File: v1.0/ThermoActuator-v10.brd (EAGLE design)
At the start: 100 x 80 mm, 76 parts, among them IC1 ULN2003AD, IC2 LM358D, IC3 LM358D, IC4 LM358D, IC5 LM358D

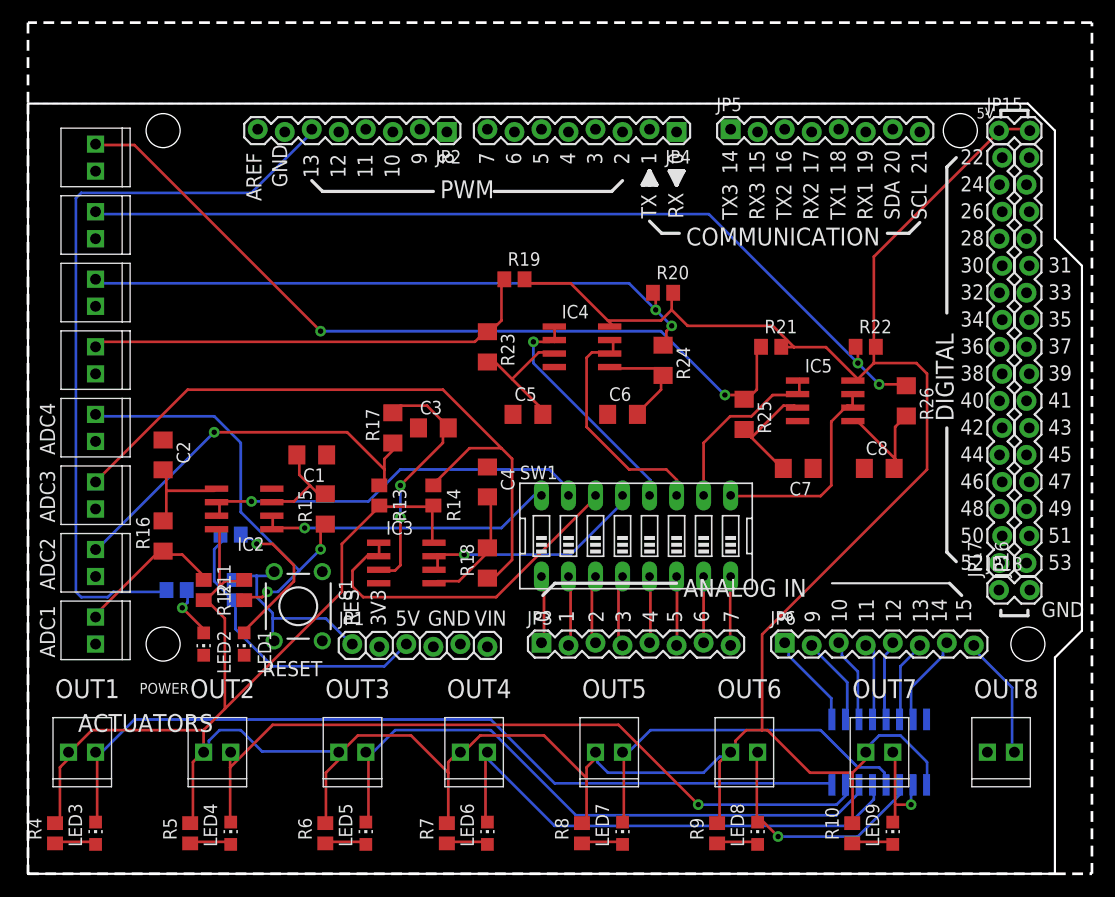
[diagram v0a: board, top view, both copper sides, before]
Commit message: local autorouting, no ripup *
almost done. Removed the reset button. Will not be used
on this shield (a higher shield will have it). Laying out
VDD route. Only local auto-route from now on
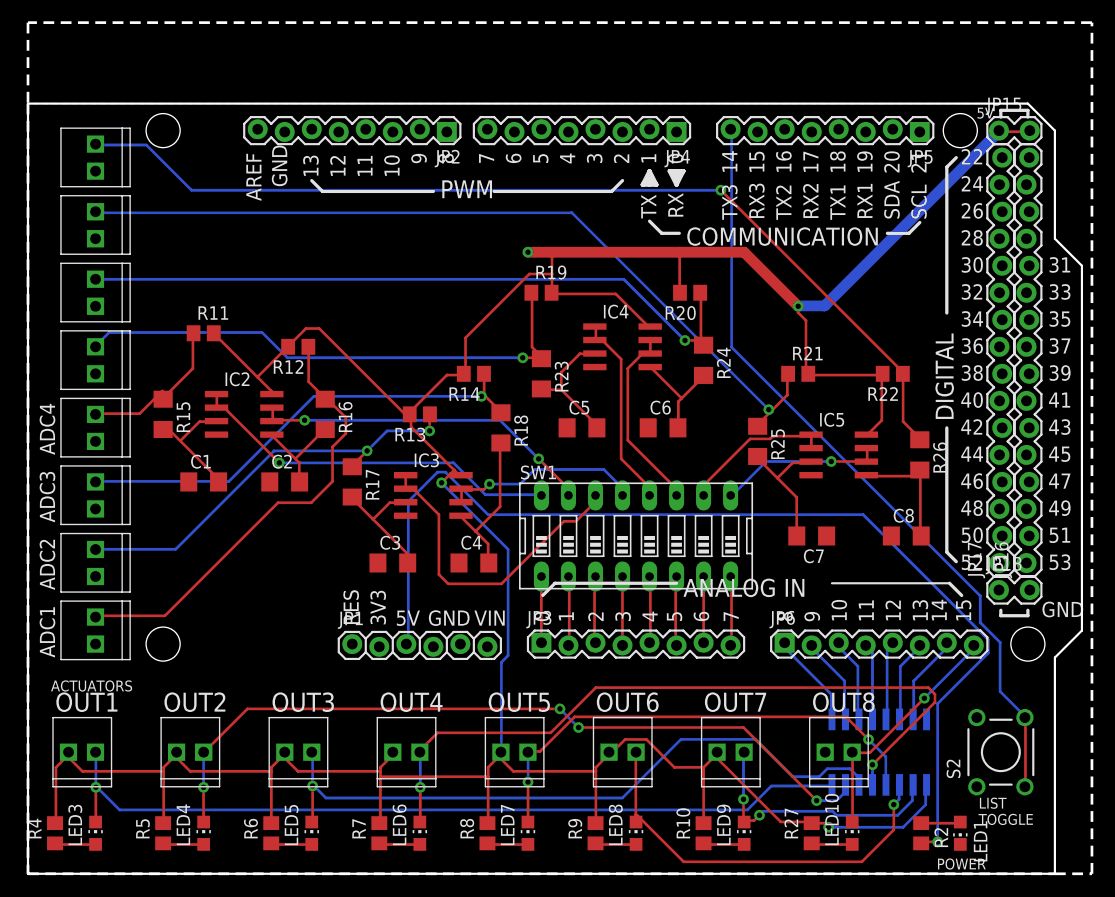
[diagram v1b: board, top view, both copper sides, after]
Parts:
- removed LED2: Green, led:CHIP-LED0805
- removed R1: (no value), rcl:R0805
- removed R3: 330, rcl:R0805
- removed S1: (no value), SparkFun:TACTILE-PTH
- added LED10: Blue, led:CHIP-LED0805
- added R27: 330, rcl:R0805
- added S2: (no value), SparkFun:TACTILE-PTH
- moved R2 70.7 mm to (83.9, 3.81), flipped to the top, turned to 270 degrees
- moved LED1 69.6 mm to (87.6, 3.81)
- moved R12 24.5 mm to (25.4, 49.5), turned to 180 degrees
- moved R11 24.4 mm to (16.5, 50.8), turned to 0 degrees
- moved R16 19.1 mm to (27.9, 43.2), turned to 270 degrees
- moved JP5 17.8 mm to (83.8, 69.8), turned to 180 degrees
- moved R15 17.6 mm to (12.7, 43.2), turned to 270 degrees
- moved JP14 15.2 mm to (77.5, 11.4)
- moved JP13 14.0 mm to (67.3, 11.4)
- moved LED9 14.0 mm to (67.3, 3.81)
- moved R10 14.0 mm to (63.5, 3.81)
- moved C3 13.3 mm to (34.3, 29.2)
- moved R18 12.8 mm to (44.5, 41.9), turned to 270 degrees
- moved R14 12.0 mm to (41.9, 47.0), turned to 180 degrees
- moved C2 11.7 mm to (24.1, 36.8), turned to 0 degrees
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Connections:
- removed net N$127: LED2.A, R3.1
- new net N$32: LED10.A, R27.1
- net 5V: no longer R1.2
- net AO7: now also LED10.C
- net D13: no longer R3.2
- net D14: now also S2.3, S2.4
- net GND: now also S2.1, S2.2; no longer LED2.C, S1.1, S1.2
- net RES: no longer R1.1, S1.3, S1.4
- net VDD: now also R27.2
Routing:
- net D14: track 0.00 -> 73.3 mm
- net D13: track 71.1 -> 0.00 mm
- net 5V: track 28.7 -> 98.3 mm, vias 0 -> 1
- net N$11: track 14.3 -> 42.4 mm
- net N$1: track 40.8 -> 15.4 mm, vias 2 -> 0
- net N$22: track 66.1 -> 44.3 mm, vias 0 -> 1
- net AO3: track 48.8 -> 68.9 mm, vias 0 -> 2
- net RES: track 19.6 -> 0.00 mm
- net AO5: track 23.2 -> 38.3 mm
- net AO6: track 10.1 -> 25.1 mm, vias 1 -> 2
- net N$21: track 24.6 -> 12.2 mm, vias 2 -> 0
- net N$126: track 14.7 -> 3.72 mm, vias 1 -> 0
- net AO7: track 11.6 -> 22.4 mm, vias 0 -> 1
- net AO4: track 35.5 -> 45.8 mm, vias 0 -> 2
- net N$30: track 84.8 -> 91.9 mm, vias 2 -> 1
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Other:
- board text added: "LIST TOGGLE"
- board text removed: "RESET"

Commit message: relay power manual route
this commit fixes one flipped connector, lines up
the connectors on 0,1mm grid (as per Mega board)

the board is almost ready for ordering
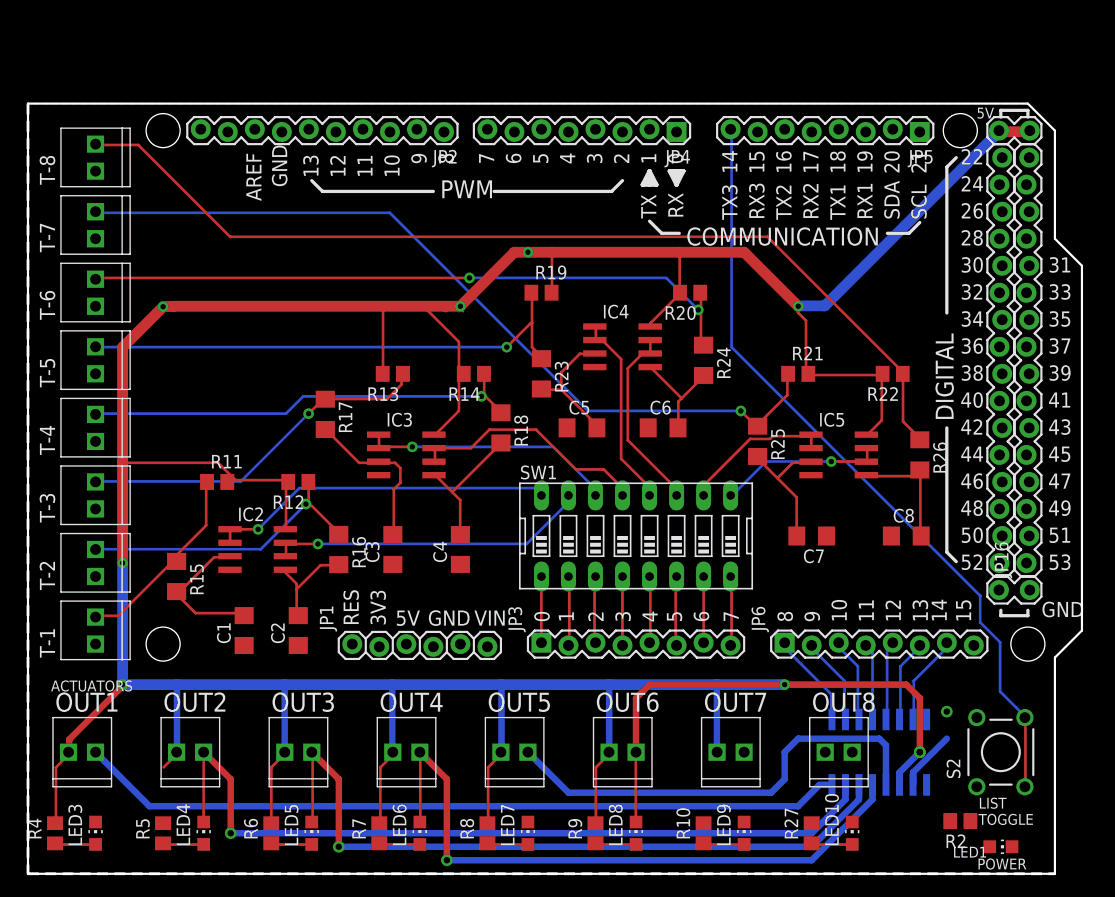
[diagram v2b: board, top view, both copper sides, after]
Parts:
- JP2: value (none) -> M10LOCK; device SparkFun:1X08_LOCK -> SparkFun-Connectors:1X10_LOCK
- moved JP19 19.1 mm to (6.35, 24.1)
- moved R15 15.3 mm to (14.0, 27.9)
- moved C1 14.5 mm to (20.3, 22.9), turned to 90 degrees
- moved C2 14.0 mm to (25.4, 22.9), turned to 90 degrees
- moved R11 14.0 mm to (17.8, 36.8)
- moved IC2 12.8 mm to (21.6, 30.5)
- moved R16 12.8 mm to (29.2, 30.5)
- moved R12 12.7 mm to (25.4, 36.8)
- moved R17 6.84 mm to (27.9, 43.2)
- moved JP20 6.35 mm to (6.35, 30.5)
- moved JP22 6.35 mm to (6.35, 43.2)
- moved JP21 6.35 mm to (6.35, 36.8)
- moved R13 4.58 mm to (34.3, 47.0)
- moved IC3 4.58 mm to (35.6, 39.4)
- moved LED1 4.02 mm to (91.4, 2.54), turned to 270 degrees
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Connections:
- net 5V: no longer R2.2
- net VDD: now also R2.2
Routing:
- net 5V: track 98.3 -> 0.00 mm, vias 1 -> 0
- net VDD: track 321.9 -> 357.7 mm, vias 4 -> 7
- net AO7: track 22.4 -> 0.00 mm, vias 1 -> 0
- net AO6: track 25.1 -> 5.66 mm, vias 2 -> 0
- net N$11: track 42.4 -> 28.0 mm, vias 0 -> 1
- net AO5: track 38.3 -> 48.3 mm
- net AO3: track 68.9 -> 61.6 mm, vias 2 -> 1
- net N$20: track 39.7 -> 33.6 mm, vias 2 -> 1
- net AS2: track 29.9 -> 24.0 mm, vias 0 -> 1
- net AO0: track 77.7 -> 72.2 mm, vias 1 -> 0
- net AO2: track 63.6 -> 68.7 mm
- net AS3: track 18.7 -> 22.8 mm, vias 1 -> 0
- net N$126: track 3.72 -> 0.00 mm
- net N$1: track 15.4 -> 18.5 mm
- net AO4: track 45.8 -> 42.8 mm, vias 2 -> 0
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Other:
- board size 100 x 80 mm -> 99.1 x 72.4 mm
- board text added: "T-1"
- board text added: "T-2"
- board text added: "T-3"
- board text added: "T-4"
- board text added: "T-5"
- board text added: "T-6"
- board text added: "T-7"
- board text added: "T-8"
- board text removed: "ADC1"
- board text removed: "ADC2"
- board text removed: "ADC3"
- board text removed: "ADC4"
- board text removed: "ANALOG IN"

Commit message: button removed. Ready for manufacturing
the button is removed. It will sit on the top layer (RTC & SD shield)

Screw terminals replace with pitch 5.

Thermistor terminals moved to upper lane

the board is ready for production, a request for quotation is sent
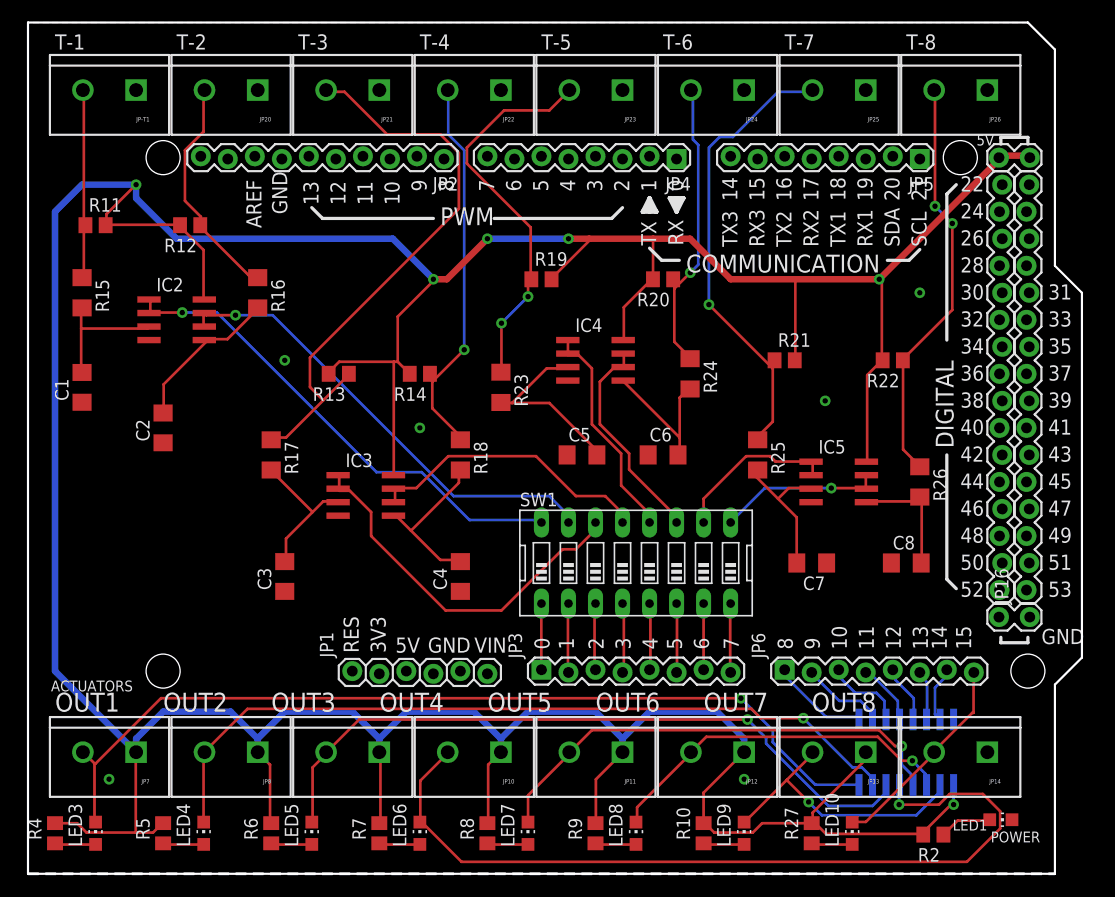
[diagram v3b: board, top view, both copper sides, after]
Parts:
- removed JP19: (no value), SparkFun-Connectors:1X02_2.54_SCREWTERM
- removed S2: (no value), SparkFun:TACTILE-PTH
- added JP-T1: M025MM, SparkFun-Connectors:SCREWTERMINAL-5MM-2
- JP10, JP11, JP12, JP13, JP14, JP20, JP21, JP22, JP23, JP24, JP25, JP26, JP7, JP8, JP9: value (none) -> M025MM; device SparkFun-Connectors:1X02_2.54_SCREWTERM -> SparkFun-Connectors:SCREWTERMINAL-5MM-2
- moved JP26 84.0 mm to (90.2, 73.7), turned to 180 degrees
- moved JP25 73.3 mm to (78.7, 73.7), turned to 180 degrees
- moved JP24 63.5 mm to (67.3, 73.7), turned to 180 degrees
- moved JP23 55.1 mm to (55.9, 73.7), turned to 180 degrees
- moved JP22 48.8 mm to (44.5, 73.7), turned to 180 degrees
- moved JP20 45.8 mm to (21.6, 73.7), turned to 180 degrees
- moved JP21 45.5 mm to (33.0, 73.7), turned to 180 degrees
- moved R15 28.1 mm to (5.08, 54.6)
- moved C1 27.5 mm to (5.08, 45.7)
- moved R11 26.7 mm to (6.35, 61.0)
- moved R12 26.2 mm to (15.2, 61.0)
- moved R16 25.3 mm to (21.6, 54.6)
- moved C2 22.9 mm to (12.7, 41.9)
- moved IC2 22.9 mm to (14.0, 52.1)
- moved JP14 12.7 mm to (90.2, 11.4)
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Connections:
- net AO0: now also JP7.2; no longer JP7.P2
- net AO1: now also JP8.2; no longer JP8.P2
- net AO2: now also JP9.2; no longer JP9.P2
- net AO3: now also JP10.2; no longer JP10.P2
- net AO4: now also JP11.2; no longer JP11.P2
- net AO5: now also JP12.2; no longer JP12.P2
- net AO6: now also JP13.2; no longer JP13.P2
- net AO7: now also JP14.2; no longer JP14.P2
- net D14: no longer S2.3, S2.4
- net GND: now also JP-T1.1, JP14.1, JP20.1, JP21.1, JP22.1, JP23.1, JP24.1, JP25.1, JP26.1; no longer JP14.P1, JP19.P1, JP20.P1, JP21.P1, JP22.P1, JP23.P1, JP24.P1, JP25.P1, JP26.P1, S2.1, S2.2
- net N$1: now also JP-T1.2; no longer JP19.P2
- net N$11: now also JP20.2; no longer JP20.P2
- net N$20: now also JP21.2; no longer JP21.P2
- net N$22: now also JP22.2; no longer JP22.P2
- net N$24: now also JP23.2; no longer JP23.P2
- net N$26: now also JP24.2; no longer JP24.P2
- net N$28: now also JP25.2; no longer JP25.P2
- net N$30: now also JP26.2; no longer JP26.P2
- net VDD: now also JP10.1, JP11.1, JP12.1, JP13.1, JP7.1, JP8.1, JP9.1; no longer JP10.P1, JP11.P1, JP12.P1, JP13.P1, JP7.P1, JP8.P1, JP9.P1
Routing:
- net D14: track 73.3 -> 0.00 mm
- net VDD: track 357.7 -> 417.3 mm, vias 7 -> 6
- net N$30: track 91.9 -> 38.7 mm, vias 0 -> 2
- net N$26: track 63.3 -> 28.0 mm, vias 2 -> 1
- net N$28: track 76.8 -> 43.5 mm
- net AO6: track 5.66 -> 26.7 mm, vias 0 -> 1
- net N$20: track 33.6 -> 54.4 mm, vias 1 -> 0
- net AO7: track 0.00 -> 19.8 mm
- net AO3: track 61.6 -> 79.2 mm
- net AO5: track 48.3 -> 34.0 mm
- net AS0: track 32.5 -> 46.5 mm
- net AS1: track 30.2 -> 44.1 mm
- net AO0: track 72.2 -> 85.5 mm, vias 0 -> 1
- net N$24: track 48.7 -> 36.7 mm, vias 1 -> 2
- net AS2: track 24.0 -> 35.5 mm, vias 1 -> 0
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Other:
- board size 99.1 x 72.4 mm -> 99.1 x 80 mm
- board text removed: "LIST TOGGLE"
